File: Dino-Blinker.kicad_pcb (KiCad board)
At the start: 2 copper layers, 63.5 x 34.4 mm, 26 parts, among them IC1 M74HC4060YRM13TR, J1 Conn_01x02_Pin

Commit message: Update Dino-Blinker.kicad_pcb
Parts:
- J1: footprint Connector_Wago:Wago_734-132_1x02_P3.50mm_Vertical -> Connector_PinHeader_2.54mm:PinHeader_1x02_P2.54mm_Vertical
- R11: value 56k -> 120k
- moved D8 1.24 mm to (155.0, 96.0)
- moved J1 0.93 mm to (141.0, 112.8), turned to -90 degrees
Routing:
- net GND: track 88.1 -> 86.8 mm
- net Net-(D8-A): track 1.76 -> 2.54 mm
- added copper zone on B.Cu, net GND
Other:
- board text added: "mitg@htl-steyr.ac.at 2024"

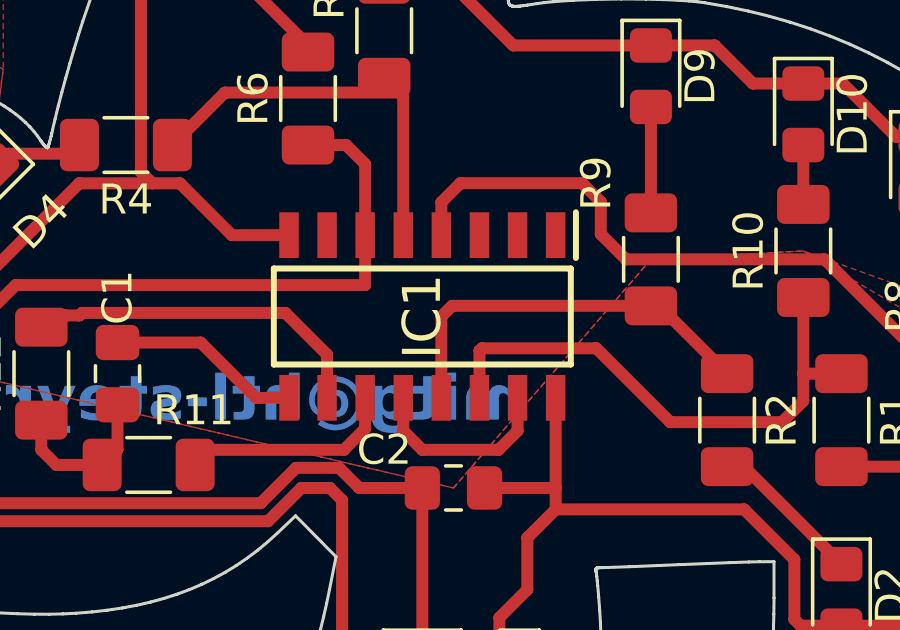
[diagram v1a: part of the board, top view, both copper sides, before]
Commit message: added folder Pics
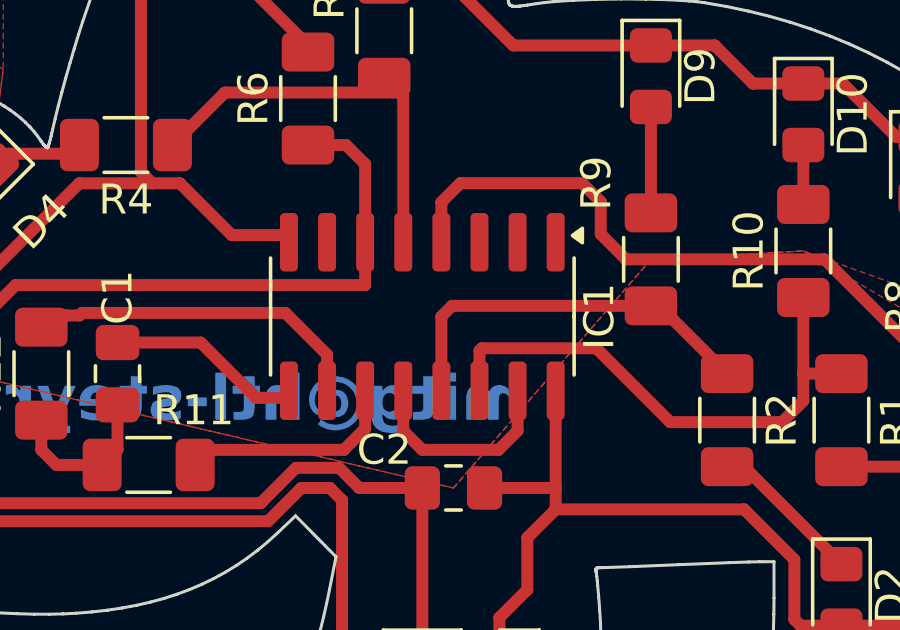
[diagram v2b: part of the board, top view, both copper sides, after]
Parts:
- IC1: footprint SamacSys_Parts:SOIC127P600X175-16N -> Package_SO:SOIC-16_3.9x9.9mm_P1.27mm
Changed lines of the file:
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@@
 		)
 	)
-	(footprint "SamacSys_Parts:SOIC127P600X175-16N"
+	(footprint "Package_SO:SOIC-16_3.9x9.9mm_P1.27mm"
 		(layer "F.Cu")
 		(at 138.43 100.965 -90)
-		(descr "ST SO-16_3")
-		(tags "Integrated Circuit")
+		(descr "SOIC, 16 Pin (JEDEC MS-012AC, https://www.analog.com/media/en/package-pcb-resources/package/pkg_pdf/soic_narrow-r/r_16.pdf), generated with kicad-footprint-generator ipc_gullwing_generator.py")
+		(tags "SOIC SO")
 		(property "Reference" "IC1"
-			(at 0 0 90)
-			(layer "F.SilkS")
-			(effects
-				(font
-					(size 1.27 1.27)
-					(thickness 0.254)
+			(at 0 -5.9 -90)
+			(layer "F.SilkS")
+			(effects
+				(font
+					(size 1 1)
+					(thickness 0.15)
 				)
 			)
 		)
 		(property "Value" "M74HC4060YRM13TR"
-			(at 0 0 90)
-			(layer "F.SilkS")
-			(hide yes)
-			(effects
-				(font
-					(size 1.27 1.27)
-					(thickness 0.254)
-				)
-			)
-		)
-		(property "Footprint" "SamacSys_Parts:SOIC127P600X175-16N"
+			(at 0 5.9 -90)
+			(layer "F.Fab")
+			(effects
+				(font
+					(size 1 1)
+					(thickness 0.15)
+				)
+			)
+		)
+		(property "Footprint" "Package_SO:SOIC-16_3.9x9.9mm_P1.27mm"
 			(at 0 0 -90)
 			(unlocked yes)
@@
 		(attr smd)
 		(fp_line
-			(start -1.6 4.95)
-			(end -1.6 -4.95)
-			(stroke
-				(width 0.2)
-				(type solid)
-			)
-			(layer "F.SilkS")
-		)
-		(fp_line
-			(start 1.6 4.95)
-			(end -1.6 4.95)
-			(stroke
-				(width 0.2)
-				(type solid)
-			)
-			(layer "F.SilkS")
-		)
-		(fp_line
-			(start -1.6 -4.95)
-			(end 1.6 -4.95)
-			(stroke
-				(width 0.2)
-				(type solid)
-			)
-			(layer "F.SilkS")
-		)
-		(fp_line
-			(start 1.6 -4.95)
-			(end 1.6 4.95)
-			(stroke
-				(width 0.2)
-				(type solid)
-			)
-			(layer "F.SilkS")
-		)
-		(fp_line
-			(start -3.475 -5.12)
-			(end -1.95 -5.12)
-			(stroke
-				(width 0.2)
-				(type solid)
-			)
-			(layer "F.SilkS")
-		)
-		(fp_line
-			(start -3.725 5.25)
-			(end -3.725 -5.25)
+			(start 0 5.06)
+			(end -1.95 5.06)
+			(stroke
+				(width 0.12)
+				(type solid)
+			)
+			(layer "F.SilkS")
+		)
+		(fp_line
+			(start 0 5.06)
+			(end 1.95 5.06)
+			(stroke
+				(width 0.12)
+				(type solid)
+			)
+			(layer "F.SilkS")
+		)
+		(fp_line
+			(start 0 -5.06)
+			(end -1.95 -5.06)
+			(stroke
+				(width 0.12)
+				(type solid)
+			)
+			(layer "F.SilkS")
+		)
+		(fp_line
+			(start 0 -5.06)
+			(end 1.95 -5.06)
+			(stroke
+				(width 0.12)
+				(type solid)
+			)
+			(layer "F.SilkS")
+		)
+		(fp_poly
+			(pts
+				(xy -2.7 -5.005) (xy -2.94 -5.335) (xy -2.46 -5.335) (xy -2.7 -5.005)
+			)
+			(stroke
+				(width 0.12)
+				(type solid)
+			)
+			(fill solid)
+			(layer "F.SilkS")
+		)
+		(fp_line
+			(start -3.7 5.2)
+			(end 3.7 5.2)
 			(stroke
 				(width 0.05)
@@
 		)
 		(fp_line
-			(start 3.725 5.25)
-			(end -3.725 5.25)
+			(start 3.7 5.2)
+			(end 3.7 -5.2)
 			(stroke
 				(width 0.05)
@@
 		)
 		(fp_line
-			(start -3.725 -5.25)
-			(end 3.725 -5.25)
+			(start -3.7 -5.2)
+			(end -3.7 5.2)
 			(stroke
 				(width 0.05)
@@
 		)
 		(fp_line
-			(start 3.725 -5.25)
-			(end 3.725 5.25)
+			(start 3.7 -5.2)
+			(end -3.7 -5.2)
 			(stroke
 				(width 0.05)
@@
 		(fp_line
 			(start -1.95 4.95)
-			(end -1.95 -4.95)
+			(end -1.95 -3.975)
 			(stroke
 				(width 0.1)
@@
 		)
 		(fp_line
-			(start -1.95 -3.68)
-			(end -0.68 -4.95)
+			(start -1.95 -3.975)
+			(end -0.975 -4.95)
 			(stroke
 				(width 0.1)
@@
 		)
 		(fp_line
-			(start -1.95 -4.95)
+			(start -0.975 -4.95)
 			(end 1.95 -4.95)
 			(stroke
@@
 		)
 		(fp_text user "${REFERENCE}"
-			(at 0 0 90)
-			(layer "F.Fab")
-			(effects
-				(font
-					(size 1.27 1.27)
-					(thickness 0.254)
-				)
-			)
-		)
-		(pad "1" smd rect
-			(at -2.712 -4.445)
-			(size 0.65 1.525)
-			(layers "F.Cu" "F.Paste" "F.Mask")
+			(at 0 0 -90)
+			(layer "F.Fab")
+			(effects
+				(font
+					(size 0.98 0.98)
+					(thickness 0.15)
+				)
+			)
+		)
+		(pad "1" smd roundrect
+			(at -2.475 -4.445 270)
+			(size 1.95 0.6)
+			(layers "F.Cu" "F.Paste" "F.Mask")
+			(roundrect_rratio 0.25)
 			(net 15 "unconnected-(IC1-Q12-Pad1)")
 			(pinfunction "Q12")
 			(pintype "passive+no_connect")
 		)
-		(pad "2" smd rect
-			(at -2.712 -3.175)
-			(size 0.65 1.525)
-			(layers "F.Cu" "F.Paste" "F.Mask")
+		(pad "2" smd roundrect
+			(at -2.475 -3.175 270)
+			(size 1.95 0.6)
+			(layers "F.Cu" "F.Paste" "F.Mask")
+			(roundrect_rratio 0.25)
 			(net 16 "unconnected-(IC1-Q13-Pad2)")
 			(pinfunction "Q13")
 			(pintype "passive+no_connect")
 		)
-		(pad "3" smd rect
-			(at -2.712 -1.905)
-			(size 0.65 1.525)
-			(layers "F.Cu" "F.Paste" "F.Mask")
+		(pad "3" smd roundrect
+			(at -2.475 -1.905 270)
+			(size 1.95 0.6)
+			(layers "F.Cu" "F.Paste" "F.Mask")
+			(roundrect_rratio 0.25)
 			(net 17 "unconnected-(IC1-Q14-Pad3)")
 			(pinfunction "Q14")
 			(pintype "passive+no_connect")
 		)
-		(pad "4" smd rect
-			(at -2.712 -0.635)
-			(size 0.65 1.525)
-			(layers "F.Cu" "F.Paste" "F.Mask")
+		(pad "4" smd roundrect
+			(at -2.475 -0.635 270)
+			(size 1.95 0.6)
+			(layers "F.Cu" "F.Paste" "F.Mask")
+			(roundrect_rratio 0.25)
 			(net 18 "/LED3")
 			(pinfunction "Q6")
 			(pintype "passive")
 		)
-		(pad "5" smd rect
-			(at -2.712 0.635)
-			(size 0.65 1.525)
-			(layers "F.Cu" "F.Paste" "F.Mask")
+		(pad "5" smd roundrect
+			(at -2.475 0.635 270)
+			(size 1.95 0.6)
+			(layers "F.Cu" "F.Paste" "F.Mask")
+			(roundrect_rratio 0.25)
 			(net 19 "/LED4")
 			(pinfunction "Q5")
 			(pintype "passive")
 		)
-		(pad "6" smd rect
-			(at -2.712 1.905)
-			(size 0.65 1.525)
-			(layers "F.Cu" "F.Paste" "F.Mask")
+		(pad "6" smd roundrect
+			(at -2.475 1.905 270)
+			(size 1.95 0.6)
+			(layers "F.Cu" "F.Paste" "F.Mask")
+			(roundrect_rratio 0.25)
 			(net 20 "/LED5")
 			(pinfunction "Q7")
 			(pintype "passive")
 		)
-		(pad "7" smd rect
-			(at -2.712 3.175)
-			(size 0.65 1.525)
-			(layers "F.Cu" "F.Paste" "F.Mask")
+		(pad "7" smd roundrect
+			(at -2.475 3.175 270)
+			(size 1.95 0.6)
+			(layers "F.Cu" "F.Paste" "F.Mask")
+			(roundrect_rratio 0.25)
 			(net 21 "unconnected-(IC1-Q4-Pad7)")
 			(pinfunction "Q4")
 			(pintype "passive+no_connect")
 		)
-		(pad "8" smd rect
-			(at -2.712 4.445)
-			(size 0.65 1.525)
-			(layers "F.Cu" "F.Paste" "F.Mask")
+		(pad "8" smd roundrect
+			(at -2.475 4.445 270)
+			(size 1.95 0.6)
+			(layers "F.Cu" "F.Paste" "F.Mask")
+			(roundrect_rratio 0.25)
 			(net 4 "GND")
 			(pinfunction "GND")
 			(pintype "power_in")
 		)
-		(pad "9" smd rect
-			(at 2.712 4.445)
-			(size 0.65 1.525)
-			(layers "F.Cu" "F.Paste" "F.Mask")
+		(pad "9" smd roundrect
+			(at 2.475 4.445 270)
+			(size 1.95 0.6)
+			(layers "F.Cu" "F.Paste" "F.Mask")
+			(roundrect_rratio 0.25)
 			(net 2 "Net-(IC1-~{[Oslash]O})")
 			(pinfunction "~{[Oslash]O}")
 			(pintype "passive")
 		)
-		(pad "10" smd rect
-			(at 2.712 3.175)
-			(size 0.65 1.525)
-			(layers "F.Cu" "F.Paste" "F.Mask")
+		(pad "10" smd roundrect
+			(at 2.475 3.175 270)
+			(size 1.95 0.6)
+			(layers "F.Cu" "F.Paste" "F.Mask")
+			(roundrect_rratio 0.25)
 			(net 22 "Net-(IC1-[Oslash]O)")
 			(pinfunction "[Oslash]O")
 			(pintype "passive")
 		)
-		(pad "11" smd rect
-			(at 2.712 1.905)
-			(size 0.65 1.525)
-			(layers "F.Cu" "F.Paste" "F.Mask")
+		(pad "11" smd roundrect
+			(at 2.475 1.905 270)
+			(size 1.95 0.6)
+			(layers "F.Cu" "F.Paste" "F.Mask")
+			(roundrect_rratio 0.25)
 			(net 23 "Net-(IC1-~{[Oslash]I})")
 			(pinfunction "~{[Oslash]I}")
 			(pintype "passive")
 		)
-		(pad "12" smd rect
-			(at 2.712 0.635)
-			(size 0.65 1.525)
-			(layers "F.Cu" "F.Paste" "F.Mask")
+		(pad "12" smd roundrect
+			(at 2.475 0.635 270)
+			(size 1.95 0.6)
+			(layers "F.Cu" "F.Paste" "F.Mask")
+			(roundrect_rratio 0.25)
 			(net 24 "Net-(IC1-CLEAR)")
 			(pinfunction "CLEAR")
 			(pintype "passive")
 		)
-		(pad "13" smd rect
-			(at 2.712 -0.635)
-			(size 0.65 1.525)
-			(layers "F.Cu" "F.Paste" "F.Mask")
+		(pad "13" smd roundrect
+			(at 2.475 -0.635 270)
+			(size 1.95 0.6)
+			(layers "F.Cu" "F.Paste" "F.Mask")
+			(roundrect_rratio 0.25)
 			(net 25 "/LED2")
 			(pinfunction "Q9")
 			(pintype "passive")
 		)
-		(pad "14" smd rect
-			(at 2.712 -1.905)
-			(size 0.65 1.525)
-			(layers "F.Cu" "F.Paste" "F.Mask")
+		(pad "14" smd roundrect
+			(at 2.475 -1.905 270)
+			(size 1.95 0.6)
+			(layers "F.Cu" "F.Paste" "F.Mask")
+			(roundrect_rratio 0.25)
 			(net 26 "/LED1")
 			(pinfunction "Q8")
 			(pintype "passive")
 		)
-		(pad "15" smd rect
-			(at 2.712 -3.175)
-			(size 0.65 1.525)
-			(layers "F.Cu" "F.Paste" "F.Mask")
+		(pad "15" smd roundrect
+			(at 2.475 -3.175 270)
+			(size 1.95 0.6)
+			(layers "F.Cu" "F.Paste" "F.Mask")
+			(roundrect_rratio 0.25)
 			(net 24 "Net-(IC1-CLEAR)")
 			(pinfunction "Q10")
 			(pintype "passive")
 		)
-		(pad "16" smd rect
-			(at 2.712 -4.445)
-			(size 0.65 1.525)
-			(layers "F.Cu" "F.Paste" "F.Mask")
+		(pad "16" smd roundrect
+			(at 2.475 -4.445 270)
+			(size 1.95 0.6)
+			(layers "F.Cu" "F.Paste" "F.Mask")
+			(roundrect_rratio 0.25)
 			(net 3 "VCC")
 			(pinfunction "VCC")
 			(pintype "power_in")
 		)
-		(model "C:\\Users\\Gerrit\\OneDrive\\Dokumente\\KiCad\\samac\\SamacSys_Parts.3dshapes\\M74HC4060YRM13TR.stp"
+		(model "${KICAD8_3DMODEL_DIR}/Package_SO.3dshapes/SOIC-16_3.9x9.9mm_P1.27mm.wrl"
 			(offset
 				(xyz 0 0 0)
